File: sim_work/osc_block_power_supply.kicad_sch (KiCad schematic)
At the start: 4 parts

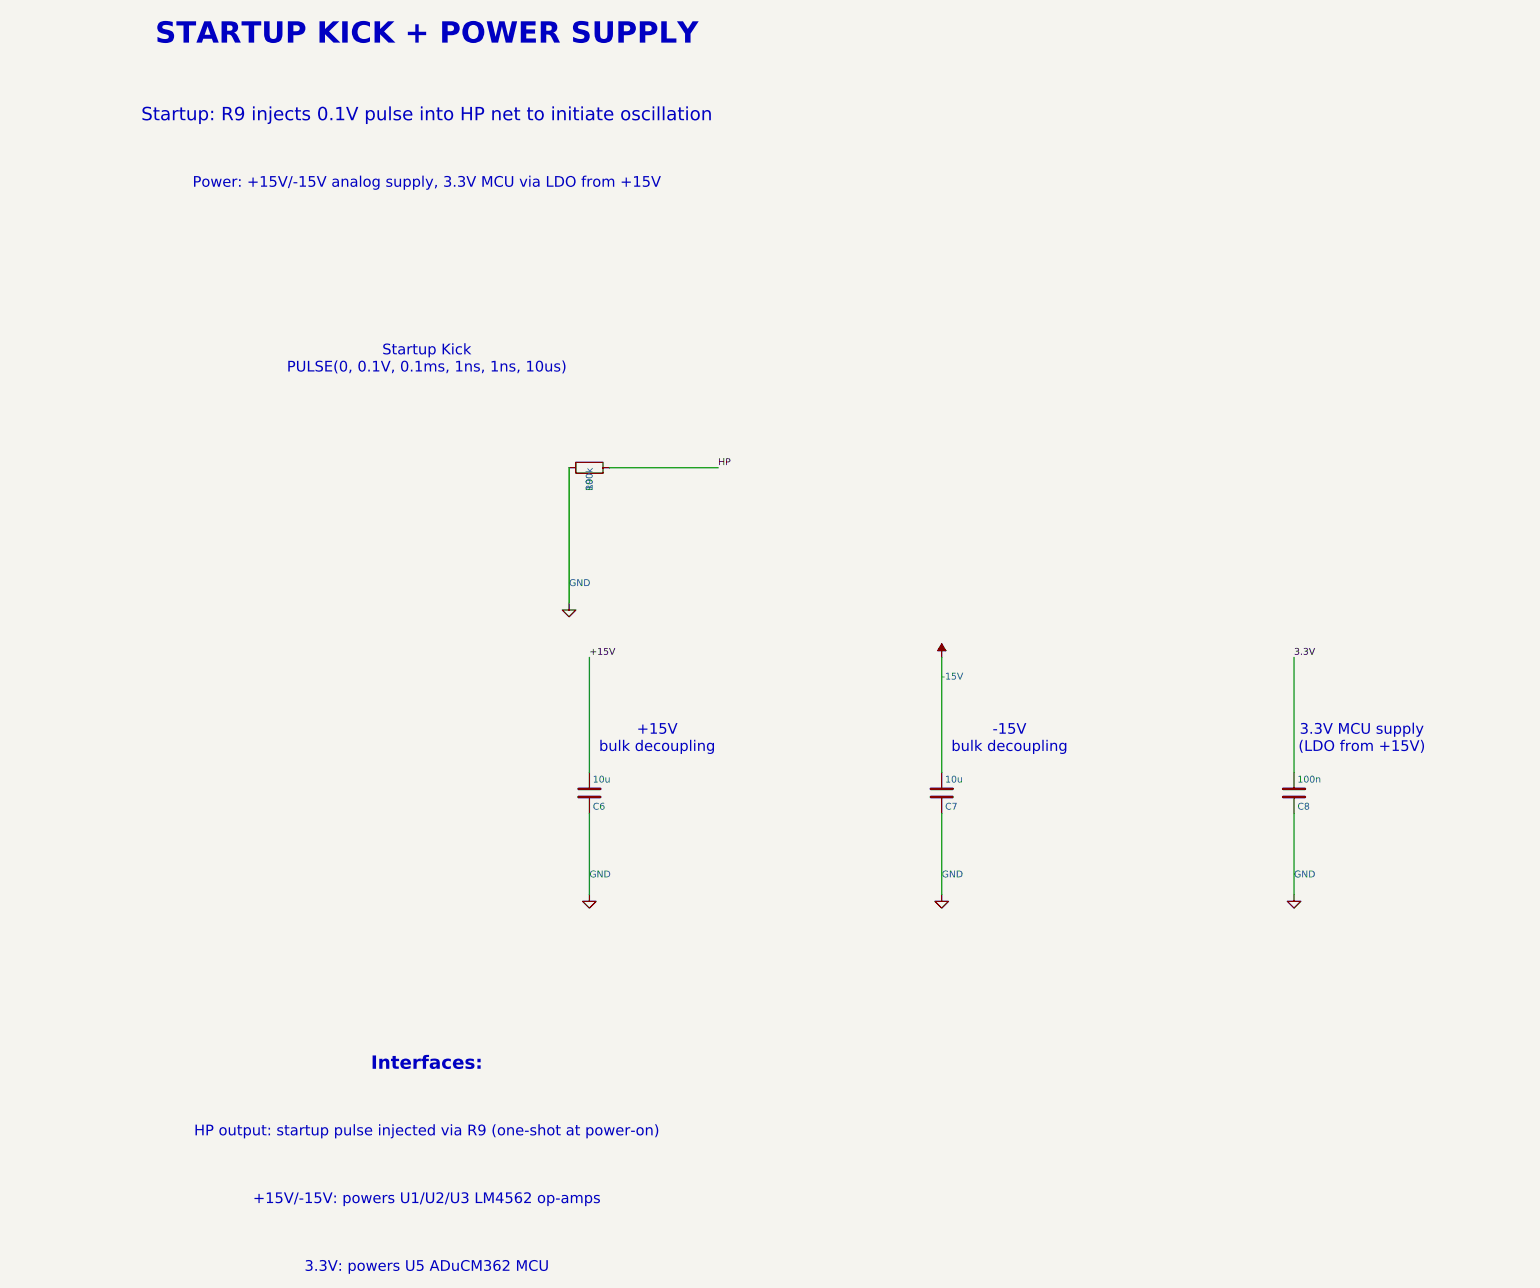
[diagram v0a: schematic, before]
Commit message: Fix schematic connections, add docs and repo portability
- Input filters: R rotation=90 (horizontal), ESD diode rotations fixed,
  junction dots at cathode-signal connection, wires to GND symbols
- Relay ladder: flyback diode rotation 270->90 (K top, A bottom)
- Electrometer/Mux TIA: 4 junction dots each at T-junctions
- AD636 RMS detector: proper IC box with pin labels replaces text-only
- Oscillator blocks: D_Zener symbol, L-shaped cathode routing
- TIA blocks: title/function annotations on all 5 blocks
- New: requirements.txt, docs/oscillator_guide.md
- D_Zener.kicad_sym added to bundled symbols/
- .gitignore updated for docs/ and requirements.txt
- README updated with pip install -r requirements.txt
- PROJECT.md session 9 changelog
- SimGUI builds clean (0 errors)

Co-Authored-By: Claude Opus 4.6 <noreply@anthropic.com>
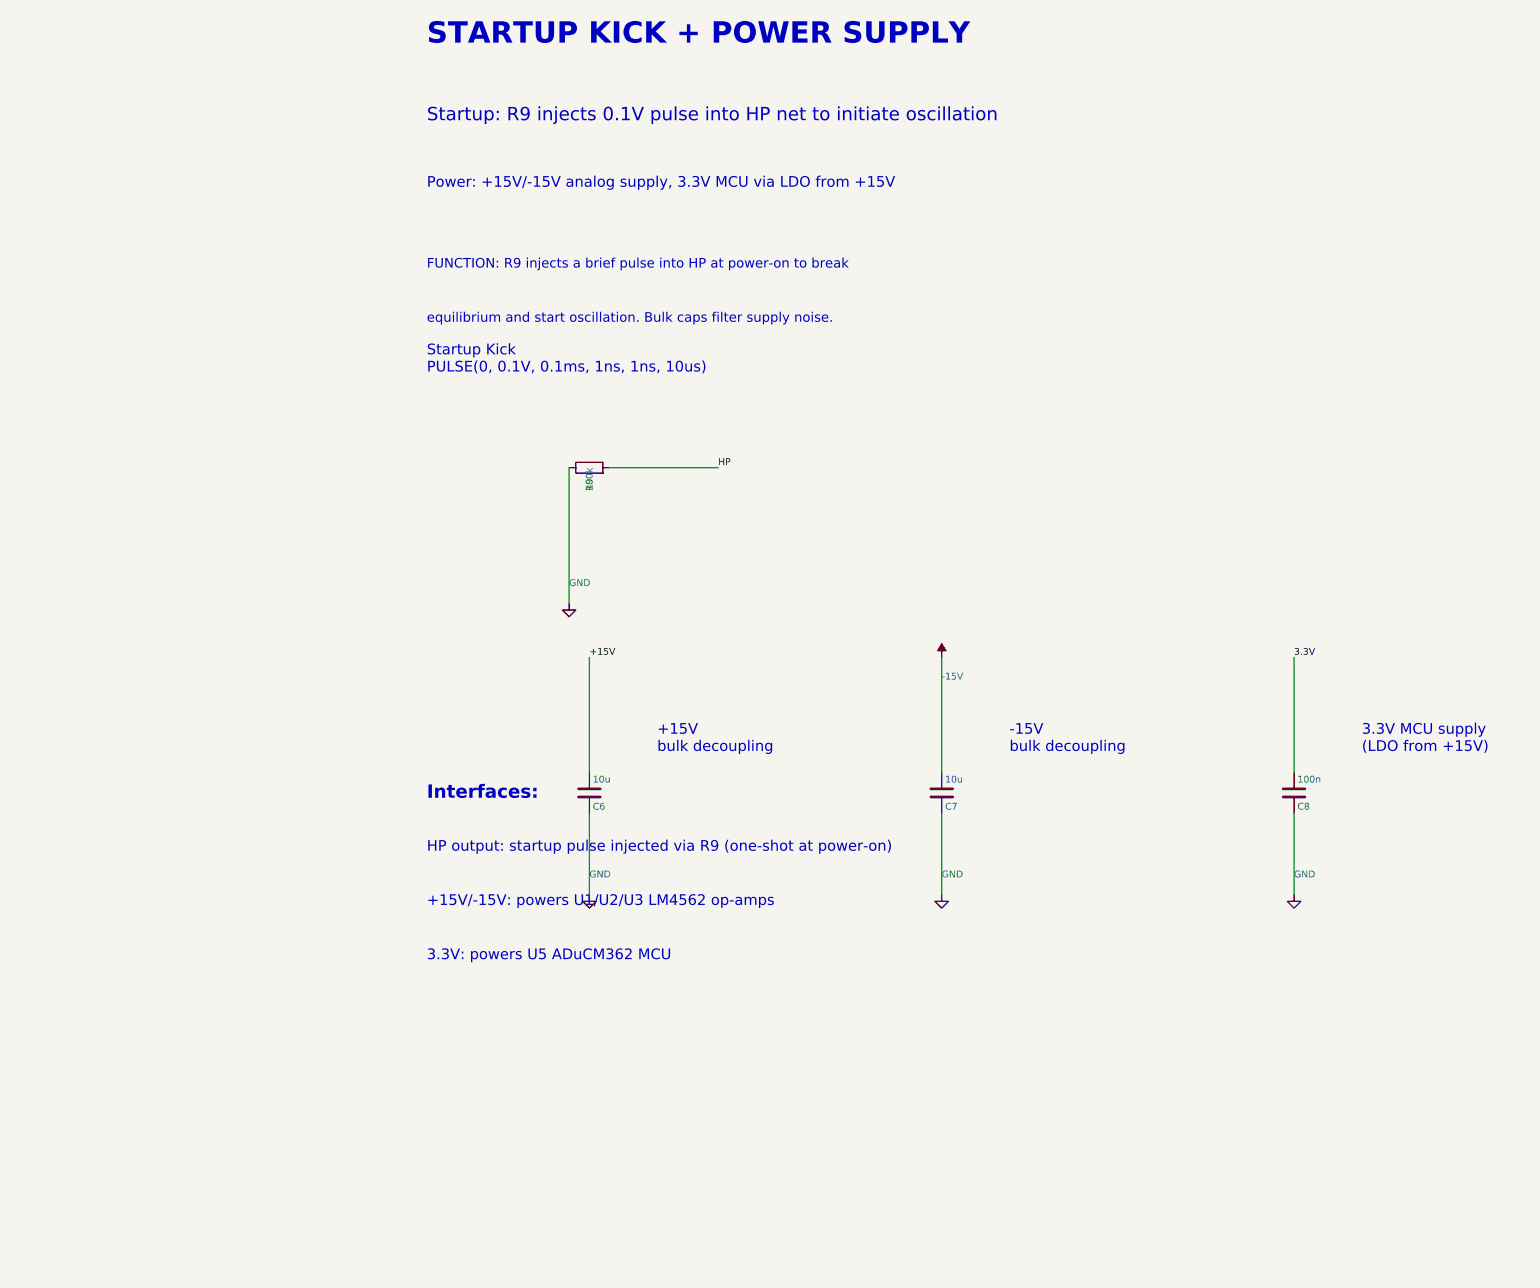
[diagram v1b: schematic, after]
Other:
- note added: "FUNCTION: R9 injects a brief pulse into HP at power-on to break"
- note added: "equilibrium and start oscillation. Bulk caps filter supply noise."
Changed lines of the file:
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@@
 		(instances
 			(project "Oscillator - Power Supply"
-				(path "/a0206bc0-a5a9-4875-8faa-8d6db68fdfb7"
+				(path "/aabb7327-2838-47f3-b749-17ca89503540"
 					(reference "R9")
 					(unit 1)
@@
 		(instances
 			(project "Oscillator - Power Supply"
-				(path "/a0206bc0-a5a9-4875-8faa-8d6db68fdfb7"
+				(path "/aabb7327-2838-47f3-b749-17ca89503540"
 					(reference "#PWR001")
 					(unit 1)
@@
 		(instances
 			(project "Oscillator - Power Supply"
-				(path "/a0206bc0-a5a9-4875-8faa-8d6db68fdfb7"
+				(path "/aabb7327-2838-47f3-b749-17ca89503540"
 					(reference "C6")
 					(unit 1)
@@
 		(instances
 			(project "Oscillator - Power Supply"
-				(path "/a0206bc0-a5a9-4875-8faa-8d6db68fdfb7"
+				(path "/aabb7327-2838-47f3-b749-17ca89503540"
 					(reference "#PWR002")
 					(unit 1)
@@
 		(instances
 			(project "Oscillator - Power Supply"
-				(path "/a0206bc0-a5a9-4875-8faa-8d6db68fdfb7"
+				(path "/aabb7327-2838-47f3-b749-17ca89503540"
 					(reference "#PWR003")
 					(unit 1)
@@
 		(instances
 			(project "Oscillator - Power Supply"
-				(path "/a0206bc0-a5a9-4875-8faa-8d6db68fdfb7"
+				(path "/aabb7327-2838-47f3-b749-17ca89503540"
 					(reference "C7")
 					(unit 1)
@@
 		(instances
 			(project "Oscillator - Power Supply"
-				(path "/a0206bc0-a5a9-4875-8faa-8d6db68fdfb7"
+				(path "/aabb7327-2838-47f3-b749-17ca89503540"
 					(reference "#PWR004")
 					(unit 1)
@@
 		(instances
 			(project "Oscillator - Power Supply"
-				(path "/a0206bc0-a5a9-4875-8faa-8d6db68fdfb7"
+				(path "/aabb7327-2838-47f3-b749-17ca89503540"
 					(reference "C8")
 					(unit 1)
@@
 		(instances
 			(project "Oscillator - Power Supply"
-				(path "/a0206bc0-a5a9-4875-8faa-8d6db68fdfb7"
+				(path "/aabb7327-2838-47f3-b749-17ca89503540"
 					(reference "#PWR005")
 					(unit 1)
@@
 				(bold yes)
 			)
+			(justify left)
 		)
 	)
@@
 				(size 2.5 2.5)
 			)
+			(justify left)
 		)
 	)
@@
 				(size 2 2)
 			)
+			(justify left)
+		)
+	)
+	(text "FUNCTION: R9 injects a brief pulse into HP at power-on to break"
+		(exclude_from_sim no)
+		(at 20.32 58.42 0.0000)
+		(effects
+			(font
+				(size 1.8 1.8)
+			)
+			(justify left)
+		)
+	)
+	(text "equilibrium and start oscillation. Bulk caps filter supply noise."
+		(exclude_from_sim no)
+		(at 20.32 68.58 0.0000)
+		(effects
+			(font
+				(size 1.8 1.8)
+			)
+			(justify left)
 		)
 	)
@@
 				(size 2 2)
 			)
+			(justify left)
 		)
 	)
@@
 				(size 2 2)
 			)
+			(justify left)
 		)
 	)
@@
 				(size 2 2)
 			)
+			(justify left)
 		)
 	)
@@
 				(size 2 2)
 			)
+			(justify left)
 		)
 	)
 	(text "Interfaces:"
 		(exclude_from_sim no)
-		(at 20.32 208.28 0.0000)
+		(at 20.32 157.48 0.0000)
 		(effects
 			(font
@@
 				(bold yes)
 			)
+			(justify left)
 		)
 	)
 	(text "HP output: startup pulse injected via R9 (one-shot at power-on)"
 		(exclude_from_sim no)
-		(at 20.32 220.98 0.0000)
-		(effects
-			(font
-				(size 2 2)
-			)
+		(at 20.32 167.64 0.0000)
+		(effects
+			(font
+				(size 2 2)
+			)
+			(justify left)
 		)
 	)
 	(text "+15V/-15V: powers U1/U2/U3 LM4562 op-amps"
 		(exclude_from_sim no)
-		(at 20.32 233.68 0.0000)
-		(effects
-			(font
-				(size 2 2)
-			)
+		(at 20.32 177.8 0.0000)
+		(effects
+			(font
+				(size 2 2)
+			)
+			(justify left)
 		)
 	)
 	(text "3.3V: powers U5 ADuCM362 MCU"
 		(exclude_from_sim no)
-		(at 20.32 246.38 0.0000)
-		(effects
-			(font
-				(size 2 2)
-			)
-		)
-	)
+		(at 20.32 187.96 0.0000)
+		(effects
+			(font
+				(size 2 2)
+			)
+			(justify left)
+		)
+	)
